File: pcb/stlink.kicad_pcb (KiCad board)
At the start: 4 copper layers, 36.5 x 20 mm, 41 parts, among them J1 USB_A, Q1 S9013, U1 XC6206P332MR, U2 STM32F103C8, Y1 8MHz

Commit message: Rev e order
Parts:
- U2: value STM32F103C8 -> STM32F103CB
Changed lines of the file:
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@@
     )
     (pad_to_mask_clearance 0)
+    (aux_axis_origin 97.13 107.24)
+    (grid_origin 97.09 107.28)
     (pcbplotparams
       (layerselection 0x00010fc_ffffffff)
@@
       (viasonmask false)
       (mode 1)
-      (useauxorigin false)
+      (useauxorigin true)
       (hpglpennumber 1)
       (hpglpenspeed 20)
@@
       (drillshape 0)
       (scaleselection 1)
-      (outputdirectory "stlink_d/")
+      (outputdirectory "stlink_e/")
     )
   )
@@
     (property "Sheetname" "")
     (attr smd)
-    (fp_text reference "C3" (at -1.5 0 unlocked) (layer "F.SilkS")
+    (fp_text reference "C3" (at -1.72 0 unlocked) (layer "F.SilkS")
       (effects (font (size 0.8 0.8) (thickness 0.15)))
     )
@@
     (property "Sheetname" "")
     (attr smd)
-    (fp_text reference "D2" (at -1.75 0 90 unlocked) (layer "F.SilkS")
+    (fp_text reference "D2" (at -1.97 0 unlocked) (layer "F.SilkS")
       (effects (font (size 0.8 0.8) (thickness 0.15)))
     )
@@
     (property "Sheetname" "")
     (attr smd)
-    (fp_text reference "D3" (at -1.75 0 90 unlocked) (layer "F.SilkS")
+    (fp_text reference "D3" (at -1.97 0 unlocked) (layer "F.SilkS")
       (effects (font (size 0.8 0.8) (thickness 0.15)))
     )
@@
     (descr "LQFP, 48 Pin (https://www.analog.com/media/en/technical-documentation/data-sheets/ltc2358-16.pdf), generated with kicad-footprint-generator ipc_gullwing_generator.py")
     (tags "LQFP QFP")
-    (property "LCSC" "C8734")
+    (property "LCSC" "C8304")
     (property "Sheetfile" "stlink.kicad_sch")
     (property "Sheetname" "")
@@
       (effects (font (size 0.8 0.8) (thickness 0.15)))
     )
-    (fp_text value "STM32F103C8" (at 0 5.85) (layer "F.Fab")
+    (fp_text value "STM32F103CB" (at 0 5.85) (layer "F.Fab")
       (effects (font (size 1 1) (thickness 0.15)))
     )
@@
     (property "Sheetname" "")
     (attr smd)
-    (fp_text reference "R1" (at 1.25 0 90 unlocked) (layer "F.SilkS")
-      (effects (font (size 0.8 0.8) (thickness 0.15)))
-    )
+    (fp_text reference "R1" (at 1.72 0 unlocked) (layer "F.SilkS")
+      (effects (font (size 0.8 0.8) (thickness 0.15)))
+    )

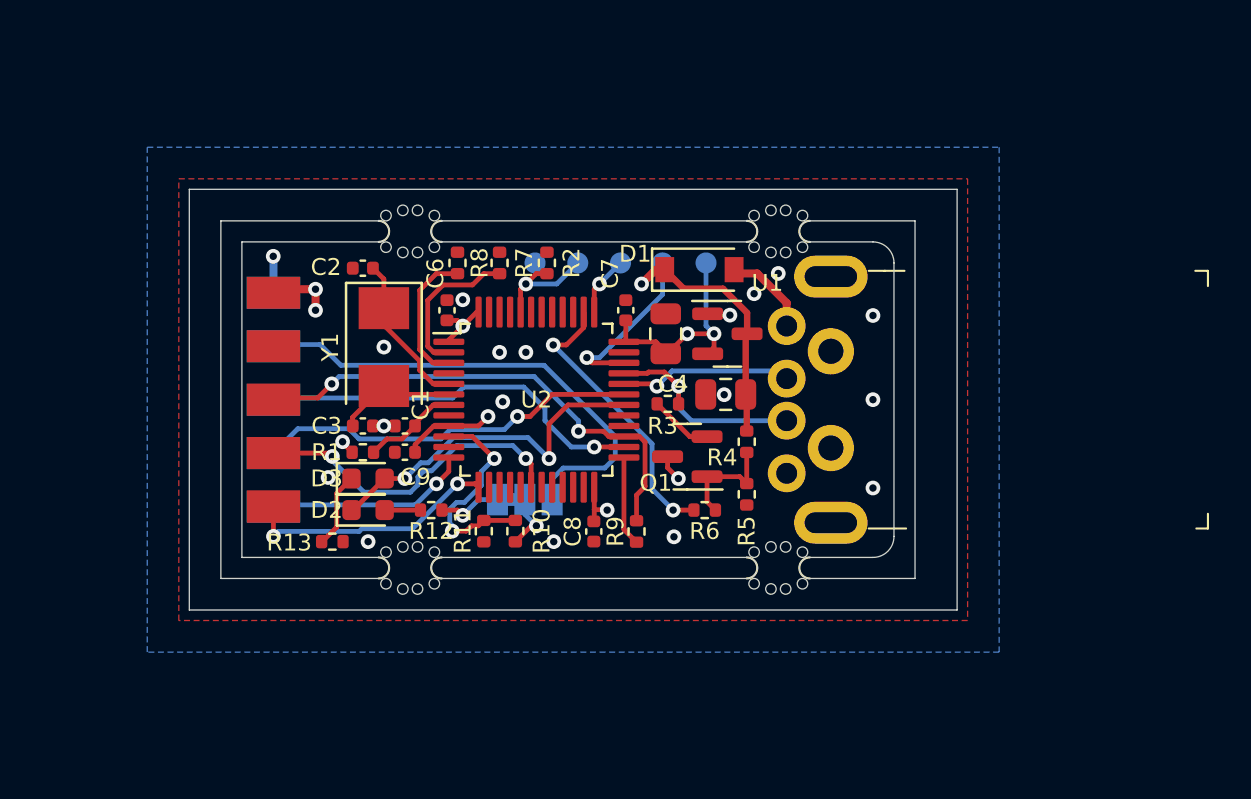
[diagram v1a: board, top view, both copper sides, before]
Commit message: Pushed new revision due to changed jlcpcb requirements.
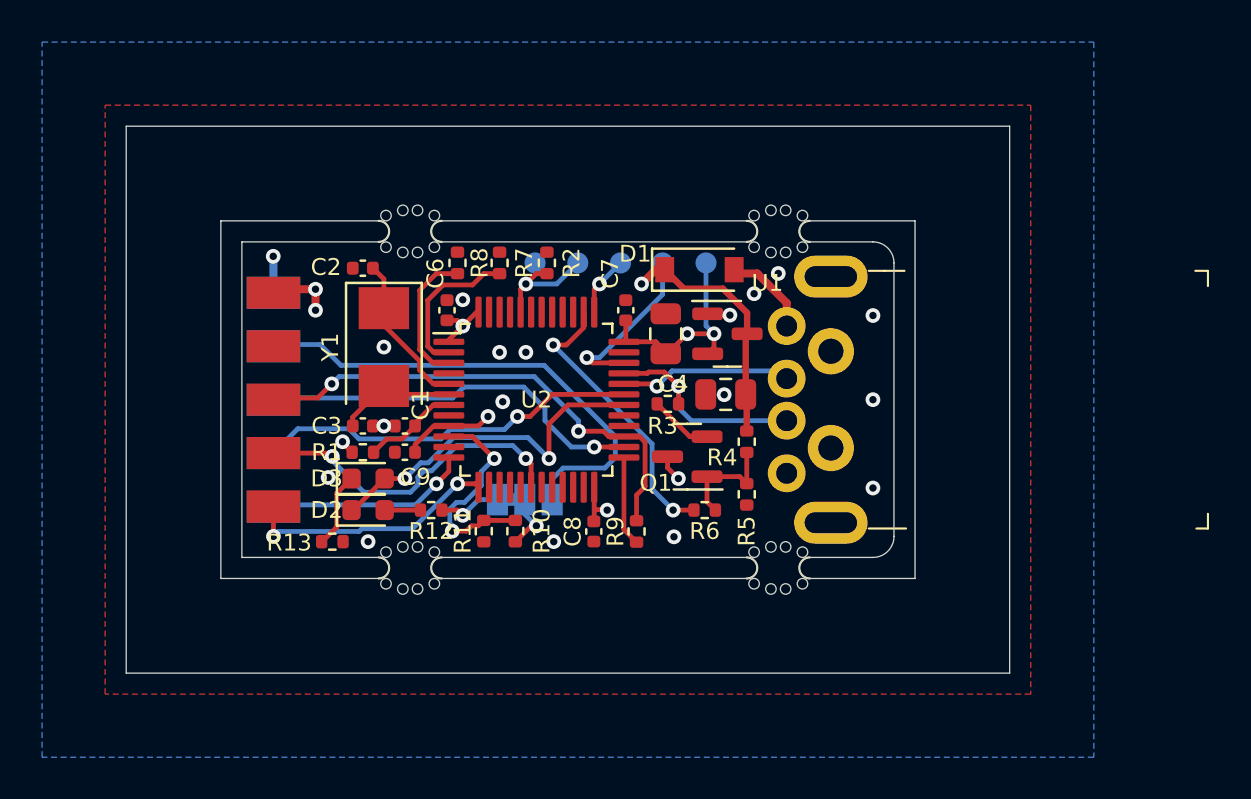
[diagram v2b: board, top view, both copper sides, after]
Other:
- board size 36.5 x 20 mm -> 42 x 26 mm
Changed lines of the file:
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@@
     )
     (pad_to_mask_clearance 0)
-    (aux_axis_origin 97.13 107.24)
-    (grid_origin 97.09 107.28)
+    (aux_axis_origin 96.5 110)
+    (grid_origin 96.5 110)
     (pcbplotparams
       (layerselection 0x00010fc_ffffffff)
@@
       (drillshape 0)
       (scaleselection 1)
-      (outputdirectory "stlink_e/")
+      (outputdirectory "stlink_f/")
     )
   )
@@
   (property "AUTHOR_EMAIL" "lth@stm32world.com")
   (property "COMPANY" "STM32World")
-  (property "REVISION" "e")
+  (property "REVISION" "f")
   (property "TITLE" "STM32 Programmer")
   (property "URL" "https://stm32world.com/wiki/DIY_STM32_Programmer_(ST-Link/V2-1)")
@@
       (net 17 "T_PWR") (pinfunction "B") (pintype "passive"))
   )
-  (gr_line (start 106.5 80) (end 143 80) (layer "Edge.Cuts") (width 0.05))
+  (gr_line (start 103.5 77) (end 145.5 77) (layer "Edge.Cuts") (width 0.05))
   (gr_line (start 133 97.5) (end 118.5 97.5) (layer "Edge.Cuts") (width 0.05))
   (gr_line (start 118.5 98.5) (end 133 98.5) (layer "Edge.Cuts") (width 0.05))
@@
   (gr_arc (start 115.5 97.5) (mid 116 98) (end 115.5 98.5) (layer "Edge.Cuts") (width 0.05))
   (gr_arc (start 118.5 82.5) (mid 118 82) (end 118.5 81.5) (layer "Edge.Cuts") (width 0.05))
-  (gr_line (start 106.5 100) (end 106.5 80) (layer "Edge.Cuts") (width 0.05))
+  (gr_line (start 103.5 103) (end 103.5 77) (layer "Edge.Cuts") (width 0.05))
   (gr_line (start 118.5 81.5) (end 133 81.5) (layer "Edge.Cuts") (width 0.05))
   (gr_line (start 133 82.5) (end 118.5 82.5) (layer "Edge.Cuts") (width 0.05))
@@
   (gr_line (start 136 82.5) (end 139 82.5) (layer "Edge.Cuts") (width 0.05))
   (gr_arc (start 133 81.5) (mid 133.5 82) (end 133 82.5) (layer "Edge.Cuts") (width 0.05))
-  (gr_line (start 143 100) (end 106.5 100) (layer "Edge.Cuts") (width 0.05))
+  (gr_line (start 145.5 103) (end 103.5 103) (layer "Edge.Cuts") (width 0.05))
   (gr_arc (start 133 97.5) (mid 133.5 98) (end 133 98.5) (layer "Edge.Cuts") (width 0.05))
   (gr_line (start 108 98.5) (end 108 81.5) (layer "Edge.Cuts") (width 0.05))
@@
   (gr_line (start 115.5 98.5) (end 108 98.5) (layer "Edge.Cuts") (width 0.05))
   (gr_line (start 115.5 82.5) (end 109 82.5) (layer "Edge.Cuts") (width 0.05))
-  (gr_line (start 143 80) (end 143 100) (layer "Edge.Cuts") (width 0.05))
+  (gr_line (start 145.5 77) (end 145.5 103) (layer "Edge.Cuts") (width 0.05))
   (gr_line (start 140 83.5) (end 140 96.5) (layer "Edge.Cuts") (width 0.05))
   (gr_text "PWR/GND" (at 112.395 87.376) (layer "B.SilkS")
@@
     (effects (font (size 0.8 0.8) (thickness 0.15)) (justify left mirror))
   )
-  (gr_text "JLCJLCJLCJLC" (at 132.25 99.25) (layer "B.SilkS")
+  (gr_text "JLCJLCJLCJLC" (at 132.5 101) (layer "B.SilkS")
     (effects (font (size 0.8 0.8) (thickness 0.15)) (justify left mirror))
   )
@@
   )
   (dimension (type aligned) (layer "Dwgs.User")
-    (pts (xy 106.5 80) (xy 106.5 100))
+    (pts (xy 103.5 77) (xy 103.5 103))
     (height 13)
-    (gr_text "20.0000 mm" (at 92.35 90 90) (layer "Dwgs.User")
+    (gr_text "26.0000 mm" (at 89.35 90 90) (layer "Dwgs.User")
       (effects (font (size 1 1) (thickness 0.15)))
     )
@@
   )
   (dimension (type aligned) (layer "Dwgs.User")
-    (pts (xy 143 80) (xy 106.5 80))
-    (height 6.5)
-    (gr_text "36.5000 mm" (at 124.75 72.35) (layer "Dwgs.User")
+    (pts (xy 145.5 77) (xy 103.5 77))
+    (height 9)
+    (gr_text "42.0000 mm" (at 124.5 66.85) (layer "Dwgs.User")
       (effects (font (size 1 1) (thickness 0.15)))
     )
@@
   (dimension (type aligned) (layer "Dwgs.User")
     (pts (xy 140 82.5) (xy 109 82.5))
-    (height 6)
-    (gr_text "31.0000 mm" (at 124.5 75.35) (layer "Dwgs.User")
+    (height 11.5)
+    (gr_text "31.0000 mm" (at 124.5 69.85) (layer "Dwgs.User")
       (effects (font (size 1 1) (thickness 0.15)))
     )
@@
     (polygon
       (pts
-        (xy 143.5 100.5)
-        (xy 106 100.5)
-        (xy 106 79.5)
-        (xy 143.5 79.5)
+        (xy 146.5 104)
+        (xy 102.5 104)
+        (xy 102.5 76)
+        (xy 146.5 76)
       )
     )
@@
     (polygon
       (pts
-        (xy 144 101)
-        (xy 105.5 101)
-        (xy 105.5 79)
-        (xy 144 79)
+        (xy 147.5 105)
+        (xy 101.5 105)
+        (xy 101.5 75)
+        (xy 147.5 75)
       )
     )
@@
     (polygon
       (pts
-        (xy 144.5 101.5)
-        (xy 105 101.5)
-        (xy 105 78.5)
-        (xy 144.5 78.5)
+        (xy 148.5 106)
+        (xy 100.5 106)
+        (xy 100.5 74)
+        (xy 148.5 74)
       )
     )
@@
     (polygon
       (pts
-        (xy 145 102)
-        (xy 104.5 102)
-        (xy 104.5 78)
-        (xy 145 78)
+        (xy 149.5 107)
+        (xy 99.5 107)
+        (xy 99.5 73)
+        (xy 149.5 73)
       )
     )

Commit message: Hmmmm
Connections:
- U2 pad 15: unconnected-(U2-Pad15) -> T_CLK
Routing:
- net T_CLK: track 18.3 -> 23.1 mm, vias 1 -> 2
- net LED: track 16.7 -> 16.2 mm
